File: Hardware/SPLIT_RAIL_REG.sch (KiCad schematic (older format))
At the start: 21 parts, among them Q1 PMOS, U1 TPS65130

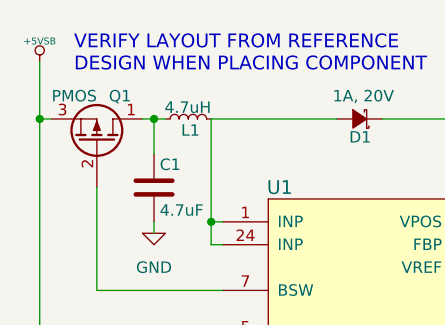
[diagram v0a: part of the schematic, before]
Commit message: Completed placement of level shifters
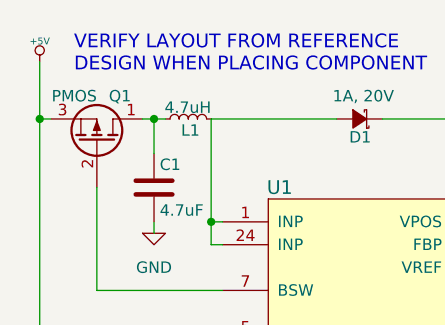
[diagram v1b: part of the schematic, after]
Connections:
- net +5VSB renamed +5V
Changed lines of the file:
@@
-	1    0    0    -1
-$EndComp
-$Comp
-L +5VSB #PWR012
-U 1 1 57F87DFC
-P 4050 2300
-F 0 "#PWR012" H 4050 2390 20  0001 C CNN
-F 1 "+5VSB" H 4050 2390 30  0000 C CNN
-F 2 "" H 4050 2300 60  0000 C CNN
-F 3 "" H 4050 2300 60  0000 C CNN
-	1    4050 2300
 	1    0    0    -1
 $EndComp
@@
 	7850 2550 7850 2300
 $Comp
-L +15VSB #PWR013
+L +15VSB #PWR012
 U 1 1 57F88166
 P 7850 2300
-F 0 "#PWR013" H 7850 2150 50  0001 C CNN
+F 0 "#PWR012" H 7850 2150 50  0001 C CNN
 F 1 "+15VSB" H 7850 2440 50  0000 C CNN
 F 2 "" H 7850 2300 50  0000 C CNN
@@
 Text Notes 6900 2950 2    60   ~ 0
 Sourced 976K\nfor R1
+$Comp
+L +5V #PWR013
+U 1 1 5862836D
+P 4050 2300
+F 0 "#PWR013" H 4050 2390 20  0001 C CNN
+F 1 "+5V" H 4050 2390 30  0000 C CNN
+F 2 "" H 4050 2300 60  0000 C CNN
+F 3 "" H 4050 2300 60  0000 C CNN
+	1    4050 2300
+	1    0    0    -1
+$EndComp
 $EndSCHEMATC

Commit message: (Digital) board fixes
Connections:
- net +5V renamed +5VSB
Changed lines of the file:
@@
 Sourced 976K\nfor R1
 $Comp
-L +5V #PWR013
-U 1 1 5862836D
+L +5VSB #PWR013
+U 1 1 586D4235
 P 4050 2300
 F 0 "#PWR013" H 4050 2390 20  0001 C CNN
-F 1 "+5V" H 4050 2390 30  0000 C CNN
+F 1 "+5VSB" H 4050 2390 30  0000 C CNN
 F 2 "" H 4050 2300 60  0000 C CNN
 F 3 "" H 4050 2300 60  0000 C CNN
